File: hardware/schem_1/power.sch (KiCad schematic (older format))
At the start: 24 parts, among them J5 UJ2-MBH-1-SMT, Q1 NDS332P, U2 XC6210B332MR, U5 XC6206-2.8V, U6 XC6206-1.2V

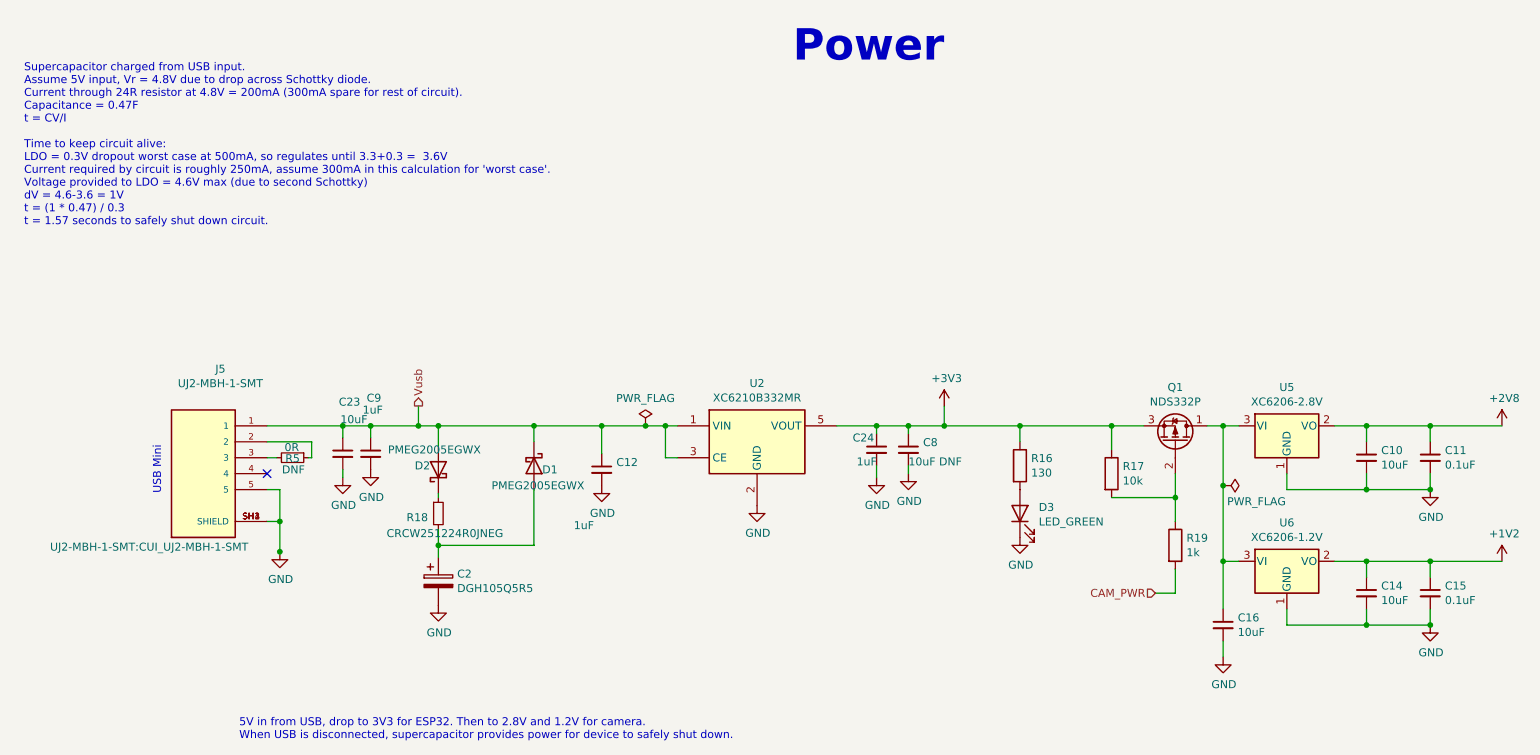
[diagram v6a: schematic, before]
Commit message: move old production stuff to new folder. start pcb spin 2: add test points (smd and pads). add third diode as currently disconnected USB can not be detected. increase LED resistor values are too bright. improve OLED footprint (to accomodate inaccuracies in drawing).
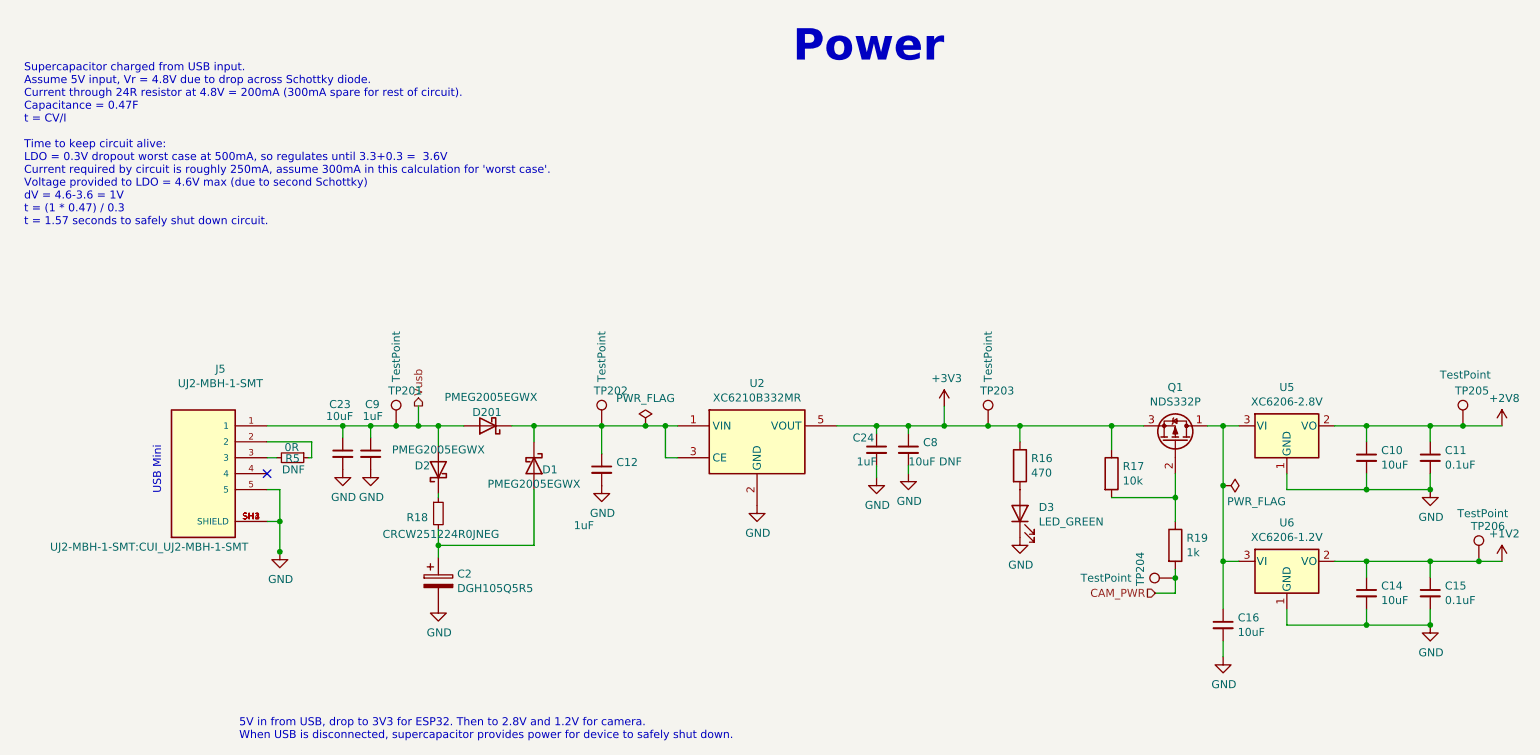
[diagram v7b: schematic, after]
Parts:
- added D201: PMEG2005EGWX, Diode_SMD:D_SOD-123, symbol Device:D_Schottky
- added TP201, TP202, TP203, TP204, TP205, TP206: TestPoint, TestPoint:TestPoint_Pad_2.0x2.0mm, symbol Connector:TestPoint
- R16: value 130 -> 470
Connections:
- net +1V2: now also TP206.1
- net +2V8: now also TP205.1
- net +3V3: now also TP203.1
- net CAM_PWR: now also TP204.1
- net Vusb: now also D201.2 (A), TP201.1; no longer C12.1, D1.1 (K), U2.1 (VIN), U2.3 (CE)
- new net: C12.1, D1.1 (K), D201.1 (K), TP202.1, U2.1 (VIN), U2.3 (CE)
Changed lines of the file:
@@
 Wire Wire Line
 	4925 3375 4850 3375
-Wire Wire Line
-	4450 3175 4725 3175
 $Comp
 L Regulator_Linear:XC6210B332MR U2
@@
 	8050 3775 8050 3625
 Wire Wire Line
-	8050 4225 8050 4075
+	8050 4225 8050 4130
 Wire Wire Line
 	8250 3175 8350 3175
@@
 Connection ~ 9650 3175
 Wire Wire Line
-	9650 3175 10100 3175
+	9650 3175 9855 3175
 $Comp
 L Device:C_Small C?
@@
 Connection ~ 9650 4025
 Wire Wire Line
-	9650 4025 10100 4025
+	9650 4025 9955 4025
 Wire Wire Line
 	8750 4325 8750 4425
@@
 Connection ~ 6600 3175
 Wire Wire Line
-	6600 3175 7075 3175
+	6600 3175 6875 3175
 Wire Wire Line
 	6375 3175 6600 3175
@@
 AR Path="/616783E5/60B19071" Ref="R16"  Part="1"
 F 0 "R16" H 7145 3471 50  0000 L CNN
-F 1 "130" H 7145 3380 50  0000 L CNN
+F 1 "470" H 7145 3380 50  0000 L CNN
 F 2 "Resistor_SMD:R_0603_1608Metric" V 7005 3425 50  0001 C CNN
 F 3 "~" H 7075 3425 50  0001 C CNN
@@
 	8350 4025 8350 4325
 Connection ~ 6375 3175
-Wire Wire Line
-	2825 3450 2825 3500
 $Comp
 L power:GND #PWR?
 U 1 1 60DA8F25
-P 2825 3500
+P 2825 3450
 AR Path="/60DA8F25" Ref="#PWR?"  Part="1"
 AR Path="/616783E5/60DA8F25" Ref="#PWR050"  Part="1"
-F 0 "#PWR050" H 2825 3250 50  0001 C CNN
-F 1 "GND" H 2830 3327 50  0000 C CNN
-F 2 "" H 2825 3500 50  0001 C CNN
-F 3 "" H 2825 3500 50  0001 C CNN
-	1    2825 3500
+F 0 "#PWR050" H 2825 3200 50  0001 C CNN
+F 1 "GND" H 2830 3277 50  0000 C CNN
+F 2 "" H 2825 3450 50  0001 C CNN
+F 3 "" H 2825 3450 50  0001 C CNN
+	1    2825 3450
 	1    0    0    -1
 $EndComp
@@
 AR Path="/60DA8C21" Ref="C?"  Part="1"
 AR Path="/616783E5/60DA8C21" Ref="C23"  Part="1"
-F 0 "C23" H 2800 3675 50  0000 L CNN
-F 1 "10uF" H 2810 3565 50  0000 L CNN
+F 0 "C23" H 2740 3660 50  0000 L CNN
+F 1 "10uF" H 2720 3585 50  0000 L CNN
 F 2 "Capacitor_SMD:C_0805_2012Metric" H 2825 3350 50  0001 C CNN
 F 3 "~" H 2825 3350 50  0001 C CNN
@@
 $EndComp
 Wire Wire Line
-	3000 3175 3300 3175
+	3000 3175 3160 3175
 $Comp
 L Device:C_Small C?
@@
 AR Path="/60AE495E" Ref="C?"  Part="1"
 AR Path="/616783E5/60AE495E" Ref="C9"  Part="1"
-F 0 "C9" H 2975 3700 50  0000 L CNN
-F 1 "1uF" H 2950 3625 50  0000 L CNN
+F 0 "C9" H 2965 3660 50  0000 L CNN
+F 1 "1uF" H 2950 3585 50  0000 L CNN
 F 2 "Capacitor_SMD:C_0603_1608Metric" H 3000 3350 50  0001 C CNN
 F 3 "~" H 3000 3350 50  0001 C CNN
@@
 AR Path="/616783E5/6169C502" Ref="D1"  Part="1"
 F 0 "D1" V 4050 3525 50  0000 C CNN
-F 1 "PMEG2005EGWX" V 4150 3450 50  0000 C CNN
+F 1 "PMEG2005EGWX" V 4140 3425 50  0000 C CNN
 F 2 "Diode_SMD:D_SOD-123" H 4025 3425 50  0001 C CNN
 F 3 "~" H 4025 3425 50  0001 C CNN
@@
 AR Path="/616783E5/6169C508" Ref="D2"  Part="1"
 F 0 "D2" V 3450 3550 50  0000 C CNN
-F 1 "PMEG2005EGWX" V 3550 3475 50  0000 C CNN
+F 1 "PMEG2005EGWX" V 3550 3450 50  0000 C CNN
 F 2 "Diode_SMD:D_SOD-123" H 3425 3450 50  0001 C CNN
 F 3 "~" H 3425 3450 50  0001 C CNN
@@
 AR Path="/616783E5/6169C511" Ref="R18"  Part="1"
 F 0 "R18" H 3225 3700 50  0000 L CNN
-F 1 "CRCW251224R0JNEG" H 3100 3600 50  0000 L CNN
+F 1 "CRCW251224R0JNEG" H 3075 3595 50  0000 L CNN
 F 2 "Resistor_SMD:R_2512_6332Metric" H 3425 3725 50  0001 C CNN
 F 3 "~" H 3425 3725 50  0001 C CNN
@@
 Connection ~ 3425 3925
 Wire Wire Line
-	3425 3175 4025 3175
+	3425 3175 3585 3175
 Connection ~ 4025 3175
 $Comp
@@
 Wire Wire Line
 	4025 3175 4450 3175
+$Comp
+L Device:D_Schottky D?
+U 1 1 6144E2D6
+P 3735 3175
+AR Path="/6144E2D6" Ref="D?"  Part="1"
+AR Path="/616783E5/6144E2D6" Ref="D201"  Part="1"
+F 0 "D201" H 3740 3090 50  0000 C CNN
+F 1 "PMEG2005EGWX" H 3715 2995 50  0000 C CNN
+F 2 "Diode_SMD:D_SOD-123" H 3735 3175 50  0001 C CNN
+F 3 "~" H 3735 3175 50  0001 C CNN
+	1    3735 3175
+	-1   0    0    1
+$EndComp
+Wire Wire Line
+	3885 3175 4025 3175
+$Comp
+L Connector:TestPoint TP201
+U 1 1 61453204
+P 3160 3175
+F 0 "TP201" H 3110 3395 50  0000 L CNN
+F 1 "TestPoint" V 3160 3450 50  0000 L CNN
+F 2 "TestPoint:TestPoint_Pad_2.0x2.0mm" H 3360 3175 50  0001 C CNN
+F 3 "~" H 3360 3175 50  0001 C CNN
+	1    3160 3175
+	1    0    0    -1
+$EndComp
+Wire Wire Line
+	4450 3175 4725 3175
+$Comp
+L Connector:TestPoint TP202
+U 1 1 61455A96
+P 4450 3175
+F 0 "TP202" H 4400 3395 50  0000 L CNN
+F 1 "TestPoint" V 4450 3450 50  0000 L CNN
+F 2 "TestPoint:TestPoint_Pad_2.0x2.0mm" H 4650 3175 50  0001 C CNN
+F 3 "~" H 4650 3175 50  0001 C CNN
+	1    4450 3175
+	1    0    0    -1
+$EndComp
+$Comp
+L Connector:TestPoint TP203
+U 1 1 614561C3
+P 6875 3175
+F 0 "TP203" H 6825 3395 50  0000 L CNN
+F 1 "TestPoint" V 6875 3450 50  0000 L CNN
+F 2 "TestPoint:TestPoint_Pad_2.0x2.0mm" H 7075 3175 50  0001 C CNN
+F 3 "~" H 7075 3175 50  0001 C CNN
+	1    6875 3175
+	1    0    0    -1
+$EndComp
+Connection ~ 6875 3175
+Wire Wire Line
+	6875 3175 7075 3175
+$Comp
+L Connector:TestPoint TP205
+U 1 1 614567B0
+P 9855 3175
+F 0 "TP205" H 9805 3395 50  0000 L CNN
+F 1 "TestPoint" H 9710 3495 50  0000 L CNN
+F 2 "TestPoint:TestPoint_Pad_2.0x2.0mm" H 10055 3175 50  0001 C CNN
+F 3 "~" H 10055 3175 50  0001 C CNN
+	1    9855 3175
+	1    0    0    -1
+$EndComp
+Connection ~ 9855 3175
+Wire Wire Line
+	9855 3175 10100 3175
+$Comp
+L Connector:TestPoint TP206
+U 1 1 61456EB7
+P 9955 4025
+F 0 "TP206" H 9905 4245 50  0000 L CNN
+F 1 "TestPoint" H 9820 4325 50  0000 L CNN
+F 2 "TestPoint:TestPoint_Pad_2.0x2.0mm" H 10155 4025 50  0001 C CNN
+F 3 "~" H 10155 4025 50  0001 C CNN
+	1    9955 4025
+	1    0    0    -1
+$EndComp
+Connection ~ 9955 4025
+Wire Wire Line
+	9955 4025 10100 4025
+$Comp
+L Connector:TestPoint TP204
+U 1 1 61457A5E
+P 8050 4130
+F 0 "TP204" H 8000 4350 50  0000 L CNN
+F 1 "TestPoint" V 8050 4405 50  0000 L CNN
+F 2 "TestPoint:TestPoint_Pad_2.0x2.0mm" H 8250 4130 50  0001 C CNN
+F 3 "~" H 8250 4130 50  0001 C CNN
+	1    8050 4130
+	0    -1   -1   0
+$EndComp
+Connection ~ 3160 3175
+Wire Wire Line
+	3160 3175 3300 3175
+Connection ~ 8050 4130
+Wire Wire Line
+	8050 4130 8050 4075
 $EndSCHEMATC
